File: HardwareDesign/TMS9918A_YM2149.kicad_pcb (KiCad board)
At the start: 2 copper layers, 150 x 90 mm, 46 parts, among them J001 Conn_02x40_Odd_Even, J701 RCJ-044, J702 Conn_01x02, J801 Conn_01x02, J802 Conn_02x09_Odd_Even, J803 SJ1-3525N, Q701 2N4401, U701 TMS9918A, U702 74HCT04, U703 74HCT32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

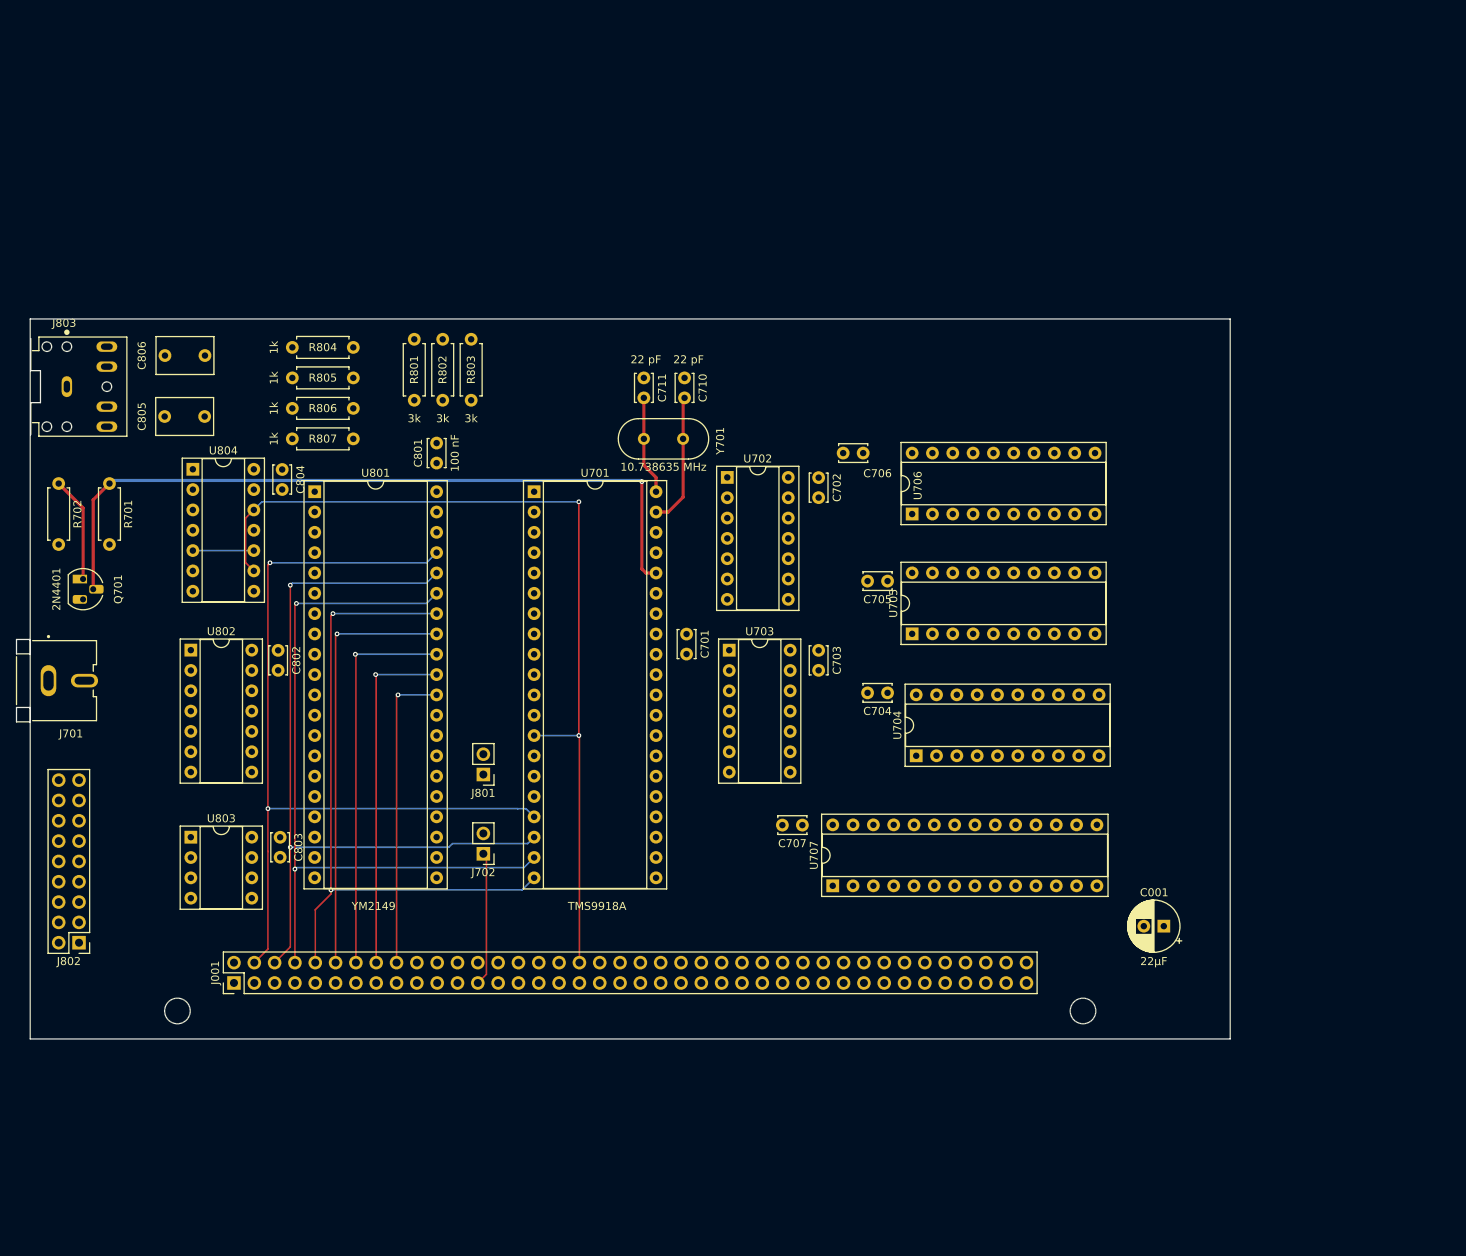
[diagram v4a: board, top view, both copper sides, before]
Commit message: routed more signals
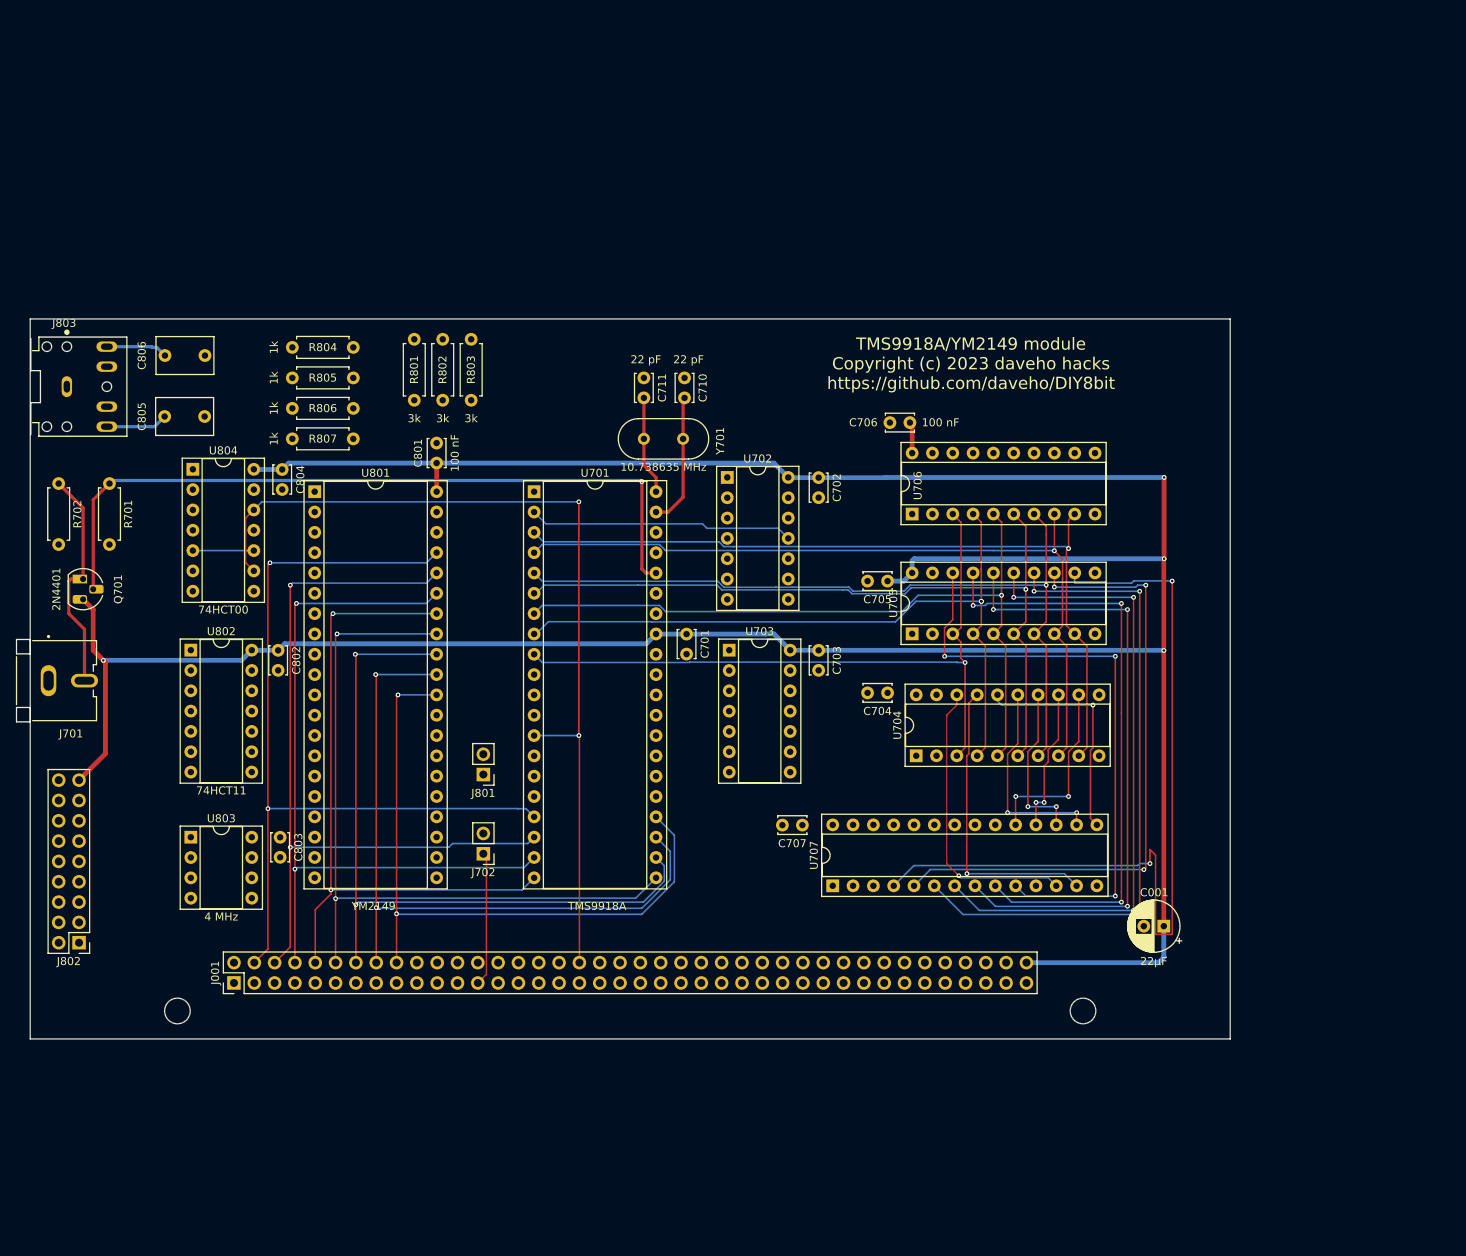
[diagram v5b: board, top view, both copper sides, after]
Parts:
- U803: value 4 MHz Osc (half can) -> 4 MHz
- moved C706 6.97 mm to (173.5, 71.4)
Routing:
- net VCC: track 0.00 -> 396.4 mm, vias 0 -> 4
- net /TMS9918ADisplay/VA6: track 0.00 -> 105.7 mm, vias 0 -> 2
- net /TMS9918ADisplay/AD7: track 0.00 -> 99.8 mm, vias 0 -> 1
- net /TMS9918ADisplay/AD6: track 0.00 -> 98.2 mm, vias 0 -> 1
- net /TMS9918ADisplay/AD5: track 0.00 -> 97.8 mm, vias 0 -> 1
- net /TMS9918ADisplay/AD4: track 0.00 -> 95.3 mm, vias 0 -> 1
- net /TMS9918ADisplay/AD3: track 0.00 -> 92.1 mm, vias 0 -> 1
- net /TMS9918ADisplay/AD2: track 0.00 -> 90.0 mm, vias 0 -> 2
- net /TMS9918ADisplay/AD1: track 0.00 -> 86.7 mm, vias 0 -> 1
- net /TMS9918ADisplay/VA4: track 0.00 -> 82.9 mm, vias 0 -> 3
- net /TMS9918ADisplay/VA3: track 0.00 -> 80.8 mm, vias 0 -> 3
- net /TMS9918ADisplay/VA2: track 0.00 -> 78.6 mm, vias 0 -> 3
- net /TMS9918ADisplay/VA5: track 0.00 -> 78.6 mm, vias 0 -> 3
- net /TMS9918ADisplay/VA1: track 0.00 -> 76.7 mm, vias 0 -> 3
- net /TMS9918ADisplay/VA0: track 0.00 -> 75.2 mm, vias 0 -> 3
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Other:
- board text added: "TMS9918A/YM2149 module Copyright (c) 2023 daveho hacks https://github.com/daveho/DIY8bit"
